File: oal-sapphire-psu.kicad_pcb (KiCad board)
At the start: 2 copper layers, 100 x 80 mm, 35 parts, among them P1 IEC, P2 LINE, P3 NEUTRAL, P4 PRIMARY_4, P5 PRIMARY_5, P6 SWITCHED_LINE, P7 OUTPUT, T1 TALEMA-25VA/12V, X1 MOUNTING_HOLE, X2 MOUNTING_HOLE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

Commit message: silk screen cleanup
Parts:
- AC IEC: renamed from P1
- F1: footprint ose-audio-labs:LITTLEFUSE-560-TR5 -> LITTLEFUSE-560-TR5
- LINE IN: renamed from P2
- T1: footprint ose-audio-labs:TALEMA_70000K_15-25VA -> TALEMA_70000K_15-25VA
- V+ OK: renamed from LED1
- V- OK: renamed from LED2
- renumbered P6 to LINE, P3 to NEUTRAL
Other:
- board text added: "120V: LINE-P4 NEUTRAL-P5 240V: NEUTRAL-P4"
- board text added: "TR5 SLOW 250V/0.5A"
- board text removed: "120V: 6-4 5-3 240V: 5-4"

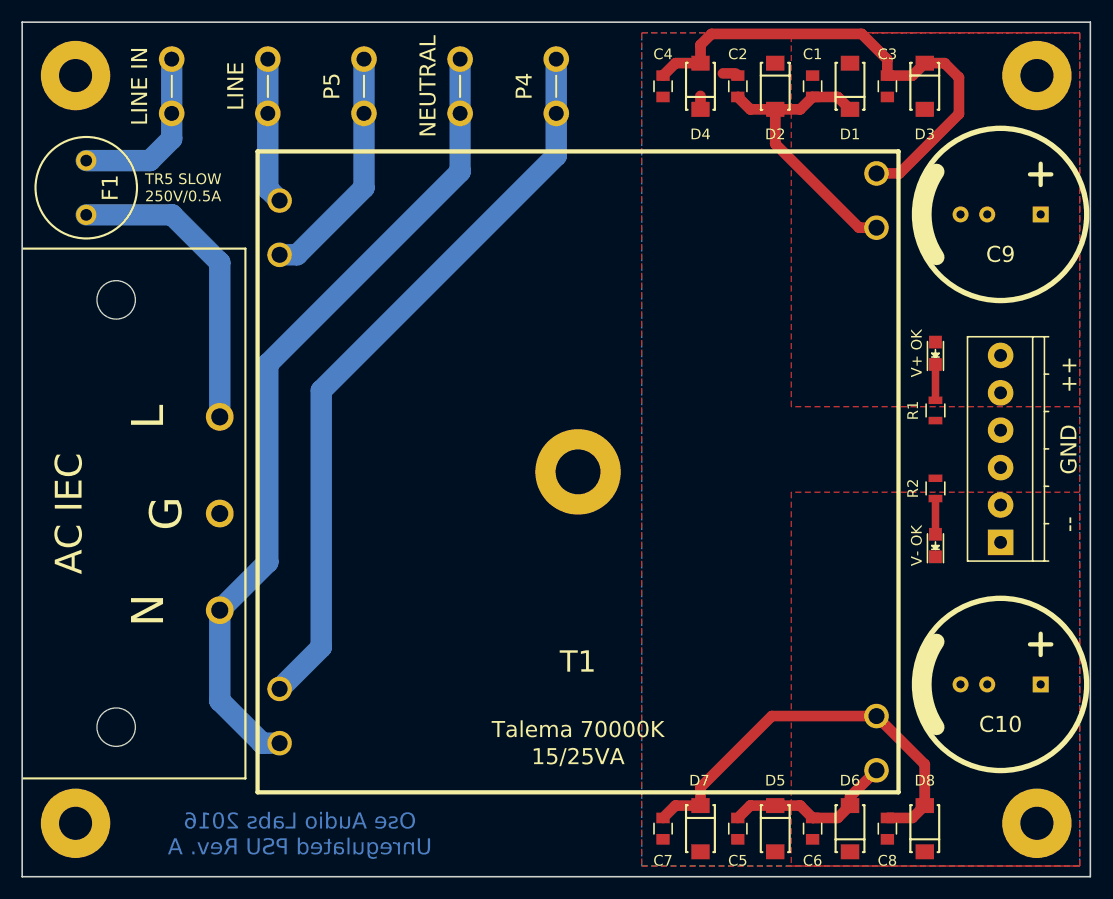
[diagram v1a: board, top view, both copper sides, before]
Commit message: updated layout
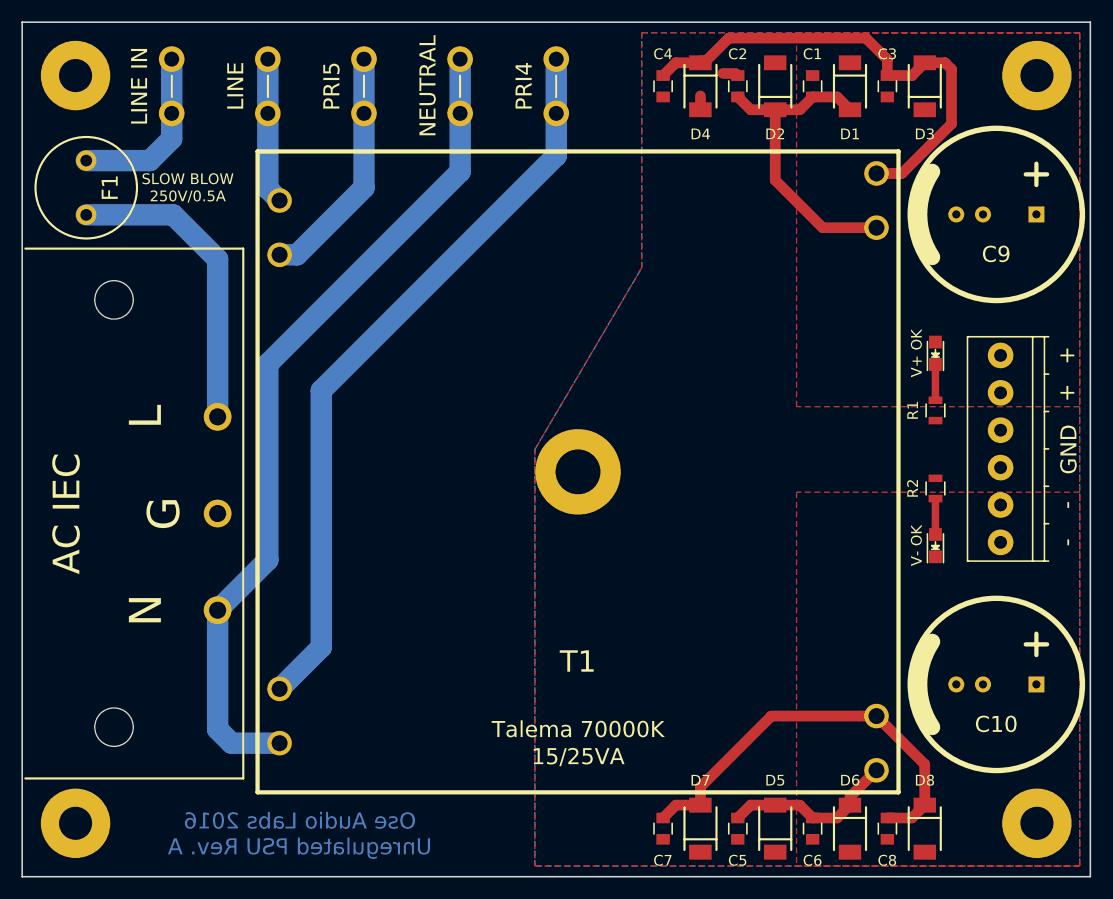
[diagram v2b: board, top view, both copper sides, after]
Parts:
- added REF**: Symbol_Highvoltage_Type1_CopperTop_Small, ose-audio-labs:Symbol_Highvoltage_Type1_SilkTop, B.Cu at (50.0, -17.0)
- AC IEC: footprint ose-audio-labs:Schurter_GSP1.8101.1 -> Schurter_GSP1.8101.1
- D1, D2, D3, D4, D5, D6, D7, D8: footprint ose-audio-labs:DO-221AC_SlimSMA -> ose-audio-labs:NXP-SOD128
- F1: footprint LITTLEFUSE-560-TR5 -> SCHURTER_FMS250V
- P7: footprint Terminal_Blocks:TerminalBlock_Pheonix_PT-3.5mm_6pol -> ose-audio-labs:TerminalBlock_Pheonix_PT-3.5mm_6pol-Vertical
- moved C10 0.40 mm to (91.2, 22.0)
- moved C9 0.40 mm to (91.2, -22.0)
- moved AC IEC 0.20 mm to (18.3, 6.00)
- renumbered P4 to PRI4, P5 to PRI5
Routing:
- net Net-(C1-Pad1): track 27.9 -> 29.9 mm
- net NEUTRAL: track 76.6 -> 78.5 mm
- net Net-(C3-Pad1): track 47.4 -> 46.1 mm
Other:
- board text added: "+"
- board text added: "-"
- board text added: "120V: LINE-PRI4 NEUTRAL-PRI5 240V: PRI5-PRI4"
- board text added: "SLOW BLOW 250V/0.5A"
- board text removed: "++"
- board text removed: "--"
- board text removed: "120V: LINE-P4 NEUTRAL-P5 240V: NEUTRAL-P4"
- board text removed: "TR5 SLOW 250V/0.5A"

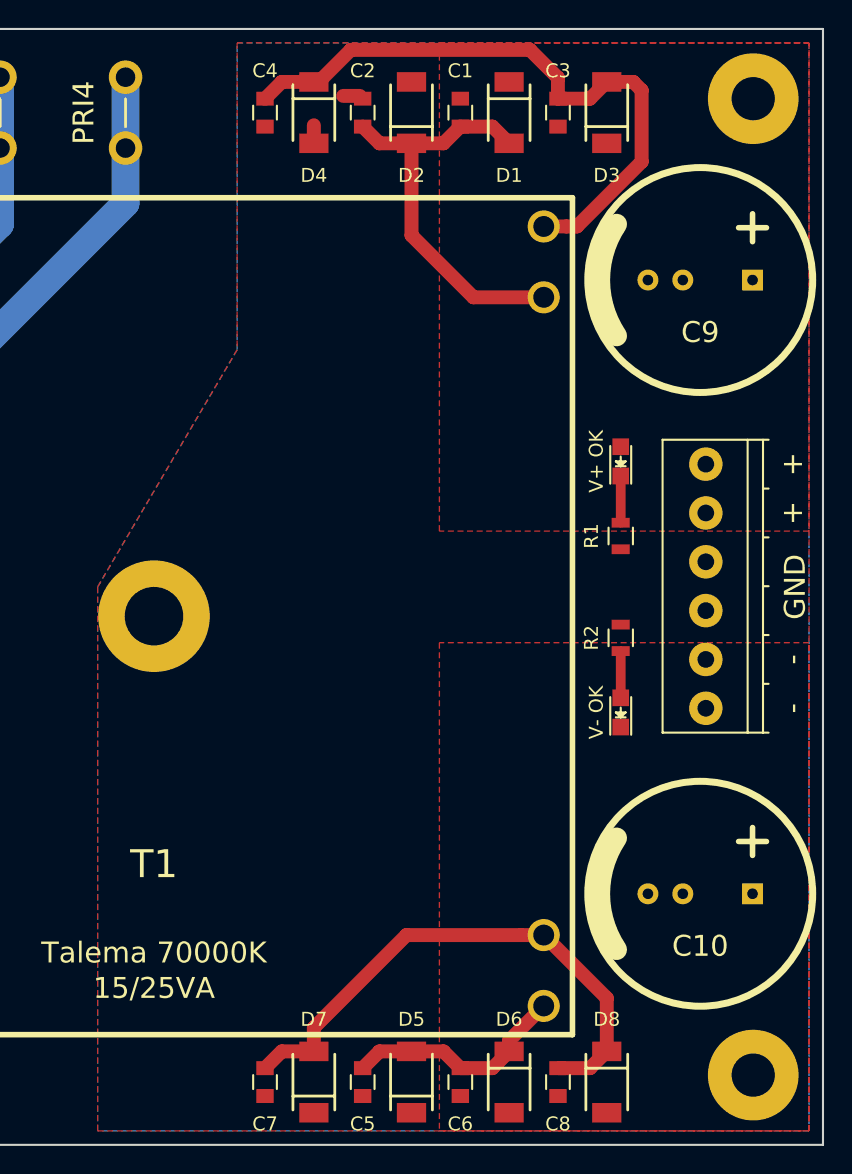
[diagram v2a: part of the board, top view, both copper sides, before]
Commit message: route all smd w/ ground pours
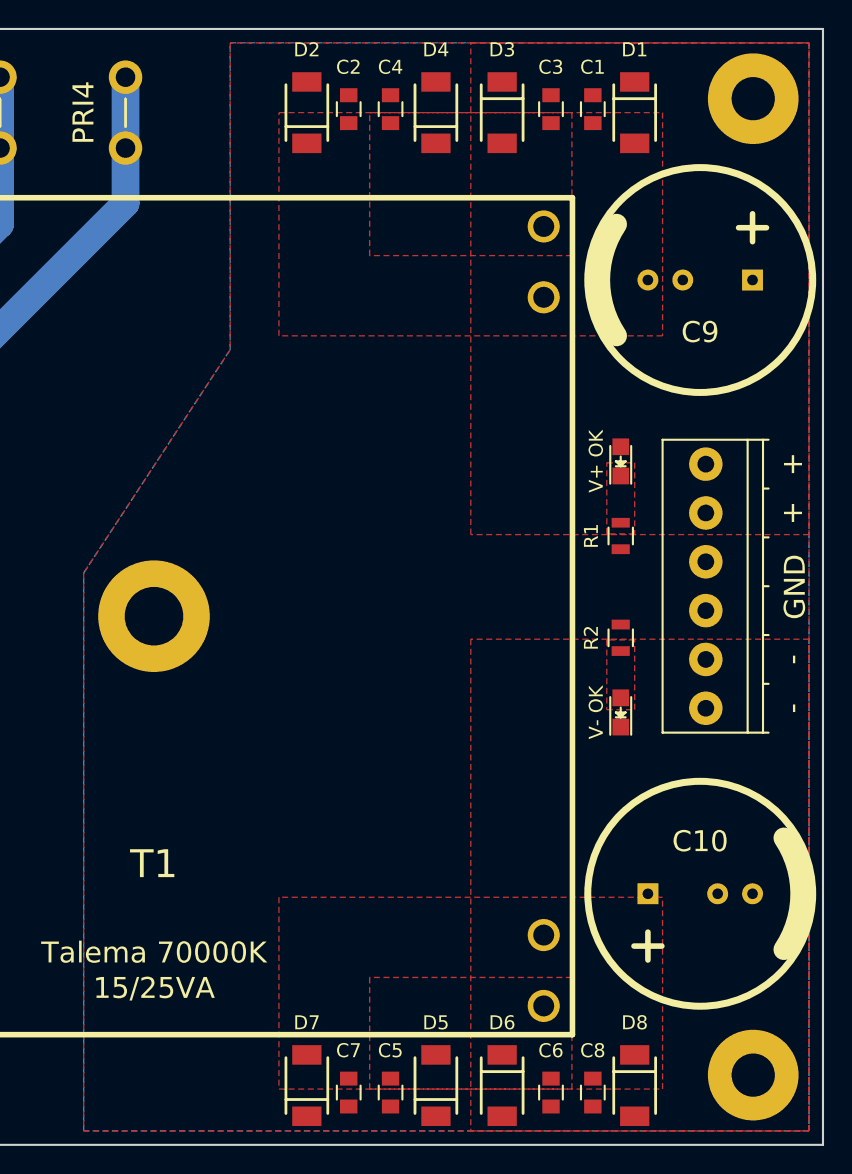
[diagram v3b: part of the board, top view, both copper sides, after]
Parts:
- moved C1 9.50 mm to (83.5, -34.2)
- moved C4 9.00 mm to (69.0, -34.2), turned to 270 degrees
- moved D1 9.00 mm to (86.5, -34.0)
- moved D4 8.75 mm to (72.2, -34.0), turned to 270 degrees
- moved D2 7.50 mm to (63.0, -34.0)
- moved D3 7.50 mm to (77.0, -34.0), turned to 90 degrees
- moved C6 6.54 mm to (80.5, 36.2)
- moved C7 6.05 mm to (66.0, 36.2)
- moved C8 2.61 mm to (83.5, 36.2)
- moved C5 2.14 mm to (69.0, 36.2)
- moved D8 2.02 mm to (86.5, 35.8)
- moved D5 1.77 mm to (72.2, 35.8)
- moved C2 1.03 mm to (66.0, -34.2)
- moved C3 0.56 mm to (80.5, -34.2), turned to 90 degrees
- moved D6 0.56 mm to (77.0, 35.8)
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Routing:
- net Net-(C3-Pad1): track 46.1 -> 0.00 mm
- net Net-(C7-Pad1): track 39.1 -> 0.00 mm
- net Net-(C1-Pad1): track 29.9 -> 0.00 mm
- net Net-(C5-Pad1): track 16.3 -> 0.00 mm
- net Net-(LED2-Pad2): track 3.35 -> 0.00 mm
- net Net-(LED1-Pad1): track 3.35 -> 0.00 mm
- net GROUND: track 2.25 -> 0.00 mm
- added copper zone on F.Cu, net Net-(C1-Pad1)
- added copper zone on F.Cu, net Net-(C3-Pad1)
- added copper zone on F.Cu, net Net-(C5-Pad1)
- added copper zone on F.Cu, net Net-(C7-Pad1)
- added copper zone on F.Cu, net Net-(LED1-Pad1)
- added copper zone on F.Cu, net Net-(LED2-Pad2)
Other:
- net class Default: clearance 0.65 -> 0.3
- net class small-pads: clearance 0.65 -> 0.3
- rule trace_clearance: 0.65 -> 0.3

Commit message: pad updates
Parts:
- LINE IN: footprint ose-audio-labs:FASTON_TAB -> FASTON_TAB
- moved P7 0.05 mm to (91.6, 8.75)
- turned C10 to 270 degrees
- turned C9 to 270 degrees

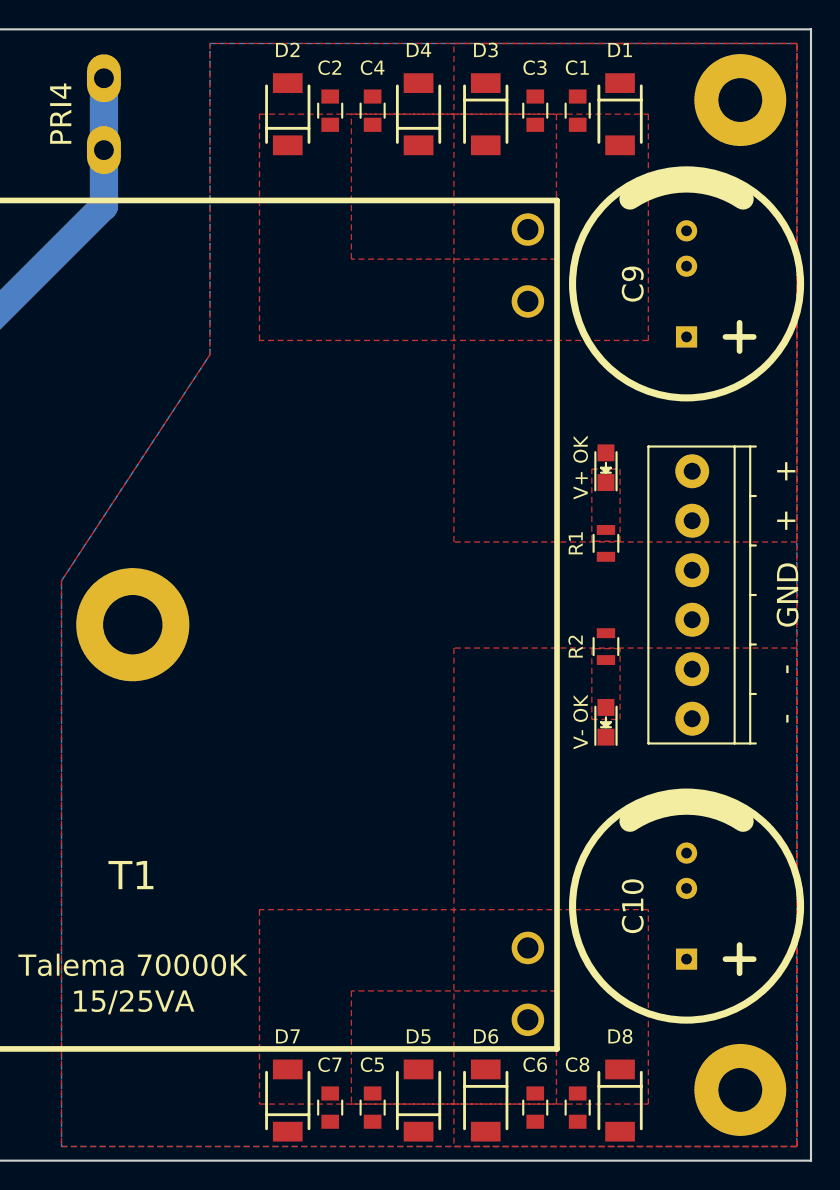
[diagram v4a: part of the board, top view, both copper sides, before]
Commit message: via stitching for ground plane
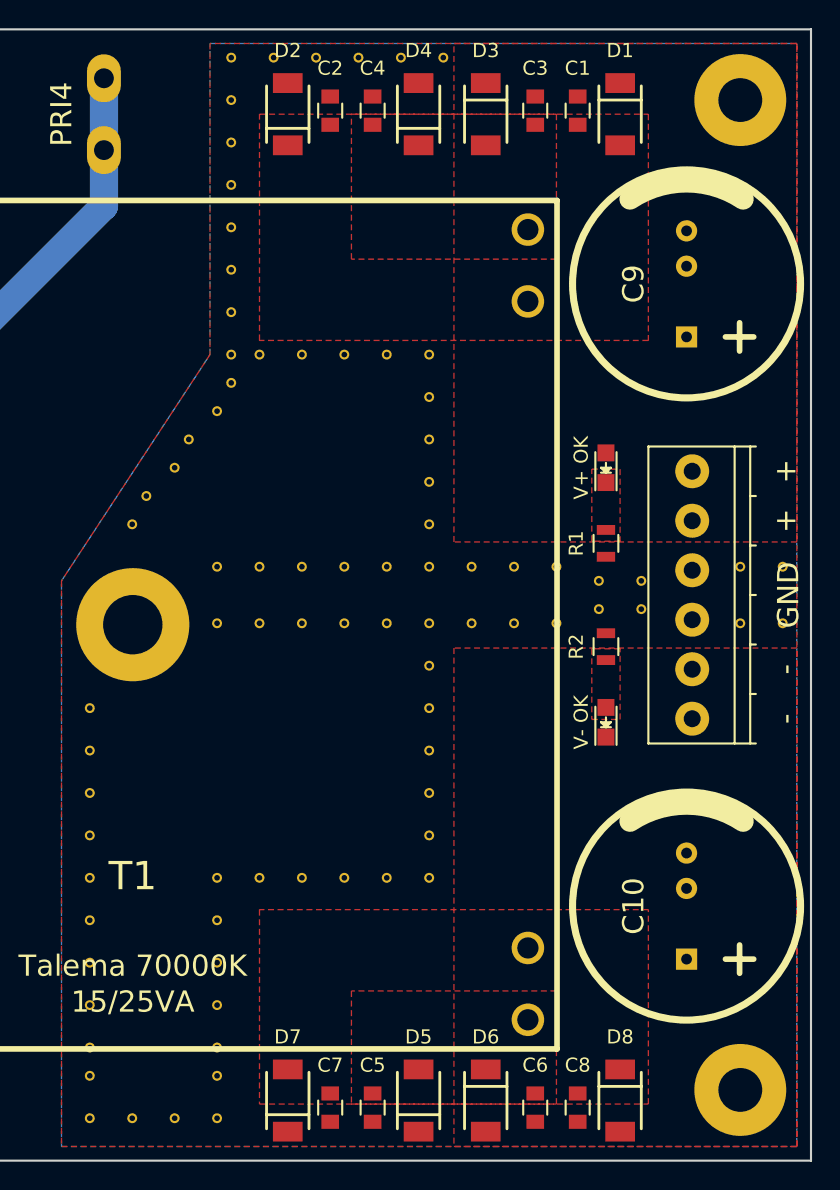
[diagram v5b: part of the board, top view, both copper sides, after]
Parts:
- added VIA-GROUND: TH-VIA, TH-VIA, F.Cu at (98.0, 2.00)
- added VIA-GROUND: TH-VIA, TH-VIA, F.Cu at (58.0, -2.00)
- added VIA-GROUND: TH-VIA, TH-VIA, F.Cu at (61.0, -2.00)
- added VIA-GROUND: TH-VIA, TH-VIA, F.Cu at (64.0, -2.00)
- added VIA-GROUND: TH-VIA, TH-VIA, F.Cu at (67.0, -2.00)
- added VIA-GROUND: TH-VIA, TH-VIA, F.Cu at (70.0, -2.00)
- added VIA-GROUND: TH-VIA, TH-VIA, F.Cu at (58.0, 32.0)
- added VIA-GROUND: TH-VIA, TH-VIA, F.Cu at (58.0, 29.0)
- added VIA-GROUND: TH-VIA, TH-VIA, F.Cu at (58.0, 26.0)
- added VIA-GROUND: TH-VIA, TH-VIA, F.Cu at (58.0, 23.0)
- added VIA-GROUND: TH-VIA, TH-VIA, F.Cu at (58.0, 20.0)
- added VIA-GROUND: TH-VIA, TH-VIA, F.Cu at (95.0, 2.00)
- added VIA-GROUND: TH-VIA, TH-VIA, F.Cu at (61.0, 20.0)
- added VIA-GROUND: TH-VIA, TH-VIA, F.Cu at (64.0, 20.0)
- added VIA-GROUND: TH-VIA, TH-VIA, F.Cu at (67.0, 20.0)
- added VIA-GROUND: TH-VIA, TH-VIA, F.Cu at (70.0, 20.0)
- added VIA-GROUND: TH-VIA, TH-VIA, F.Cu at (73.0, 20.0)
- added VIA-GROUND: TH-VIA, TH-VIA, F.Cu at (73.0, 17.0)
- added VIA-GROUND: TH-VIA, TH-VIA, F.Cu at (73.0, 14.0)
- added VIA-GROUND: TH-VIA, TH-VIA, F.Cu at (73.0, 11.0)
- added VIA-GROUND: TH-VIA, TH-VIA, F.Cu at (73.0, 8.00)
- added VIA-GROUND: TH-VIA, TH-VIA, F.Cu at (73.0, 5.00)
- added VIA-GROUND: TH-VIA, TH-VIA, F.Cu at (95.0, -2.00)
- added VIA-GROUND: TH-VIA, TH-VIA, F.Cu at (73.0, 2.00)
- added VIA-GROUND: TH-VIA, TH-VIA, F.Cu at (76.0, 2.00)
- added VIA-GROUND: TH-VIA, TH-VIA, F.Cu at (79.0, 2.00)
- added VIA-GROUND: TH-VIA, TH-VIA, F.Cu at (82.0, 2.00)
- added VIA-GROUND: TH-VIA, TH-VIA, F.Cu at (85.0, 1.00)
- added VIA-GROUND: TH-VIA, TH-VIA, F.Cu at (88.0, 1.00)
- added VIA-GROUND: TH-VIA, TH-VIA, F.Cu at (88.0, -1.00)
- added VIA-GROUND: TH-VIA, TH-VIA, F.Cu at (85.0, -1.00)
- added VIA-GROUND: TH-VIA, TH-VIA, F.Cu at (82.0, -2.00)
- added VIA-GROUND: TH-VIA, TH-VIA, F.Cu at (79.0, -2.00)
- added VIA-GROUND: TH-VIA, TH-VIA, F.Cu at (98.0, -2.00)
- added VIA-GROUND: TH-VIA, TH-VIA, F.Cu at (76.0, -2.00)
- added VIA-GROUND: TH-VIA, TH-VIA, F.Cu at (73.0, -2.00)
- added VIA-GROUND: TH-VIA, TH-VIA, F.Cu at (73.0, -5.00)
- added VIA-GROUND: TH-VIA, TH-VIA, F.Cu at (73.0, -8.00)
- added VIA-GROUND: TH-VIA, TH-VIA, F.Cu at (73.0, -11.0)
- added VIA-GROUND: TH-VIA, TH-VIA, F.Cu at (73.0, -14.0)
- added VIA-GROUND: TH-VIA, TH-VIA, F.Cu at (73.0, -17.0)
- added VIA-GROUND: TH-VIA, TH-VIA, F.Cu at (70.0, -17.0)
- added VIA-GROUND: TH-VIA, TH-VIA, F.Cu at (67.0, -17.0)
- added VIA-GROUND: TH-VIA, TH-VIA, F.Cu at (64.0, -17.0)
- added VIA-GROUND: TH-VIA, TH-VIA, F.Cu at (70.0, 2.00)
- added VIA-GROUND: TH-VIA, TH-VIA, F.Cu at (61.0, -17.0)
- added VIA-GROUND: TH-VIA, TH-VIA, F.Cu at (59.0, -17.0)
- added VIA-GROUND: TH-VIA, TH-VIA, F.Cu at (59.0, -20.0)
- added VIA-GROUND: TH-VIA, TH-VIA, F.Cu at (59.0, -23.0)
- added VIA-GROUND: TH-VIA, TH-VIA, F.Cu at (49.0, 11.0)
- added VIA-GROUND: TH-VIA, TH-VIA, F.Cu at (49.0, 8.00)
- added VIA-GROUND: TH-VIA, TH-VIA, F.Cu at (49.0, 14.0)
- added VIA-GROUND: TH-VIA, TH-VIA, F.Cu at (49.0, 17.0)
- added VIA-GROUND: TH-VIA, TH-VIA, F.Cu at (49.0, 20.0)
- added VIA-GROUND: TH-VIA, TH-VIA, F.Cu at (49.0, 23.0)
- added VIA-GROUND: TH-VIA, TH-VIA, F.Cu at (67.0, 2.00)
- added VIA-GROUND: TH-VIA, TH-VIA, F.Cu at (49.0, 26.0)
- added VIA-GROUND: TH-VIA, TH-VIA, F.Cu at (58.0, 34.0)
- added VIA-GROUND: TH-VIA, TH-VIA, F.Cu at (74.0, -38.0)
- added VIA-GROUND: TH-VIA, TH-VIA, F.Cu at (71.0, -38.0)
- added VIA-GROUND: TH-VIA, TH-VIA, F.Cu at (59.0, -29.0)
- added VIA-GROUND: TH-VIA, TH-VIA, F.Cu at (59.0, -15.0)
- added VIA-GROUND: TH-VIA, TH-VIA, F.Cu at (52.0, -5.00)
- added VIA-GROUND: TH-VIA, TH-VIA, F.Cu at (65.0, -38.0)
- added VIA-GROUND: TH-VIA, TH-VIA, F.Cu at (68.0, -38.0)
- added VIA-GROUND: TH-VIA, TH-VIA, F.Cu at (62.0, -38.0)
- added VIA-GROUND: TH-VIA, TH-VIA, F.Cu at (64.0, 2.00)
- added VIA-GROUND: TH-VIA, TH-VIA, F.Cu at (59.0, -26.0)
- added VIA-GROUND: TH-VIA, TH-VIA, F.Cu at (59.0, -32.0)
- added VIA-GROUND: TH-VIA, TH-VIA, F.Cu at (59.0, -35.0)
- added VIA-GROUND: TH-VIA, TH-VIA, F.Cu at (59.0, -38.0)
- added VIA-GROUND: TH-VIA, TH-VIA, F.Cu at (58.0, 37.0)
- added VIA-GROUND: TH-VIA, TH-VIA, F.Cu at (56.0, -11.0)
- added VIA-GROUND: TH-VIA, TH-VIA, F.Cu at (58.0, -13.0)
- added VIA-GROUND: TH-VIA, TH-VIA, F.Cu at (55.0, -9.00)
- added VIA-GROUND: TH-VIA, TH-VIA, F.Cu at (49.0, 32.0)
- added VIA-GROUND: TH-VIA, TH-VIA, F.Cu at (53.0, -7.00)
- added VIA-GROUND: TH-VIA, TH-VIA, F.Cu at (61.0, 2.00)
- added VIA-GROUND: TH-VIA, TH-VIA, F.Cu at (55.0, 37.0)
- added VIA-GROUND: TH-VIA, TH-VIA, F.Cu at (52.0, 37.0)
- added VIA-GROUND: TH-VIA, TH-VIA, F.Cu at (49.0, 29.0)
- added VIA-GROUND: TH-VIA, TH-VIA, F.Cu at (49.0, 34.0)
- added VIA-GROUND: TH-VIA, TH-VIA, F.Cu at (49.0, 37.0)
- added VIA-GROUND: TH-VIA, TH-VIA, F.Cu at (58.0, 2.00)
